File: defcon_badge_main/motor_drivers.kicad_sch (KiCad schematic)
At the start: 14 parts

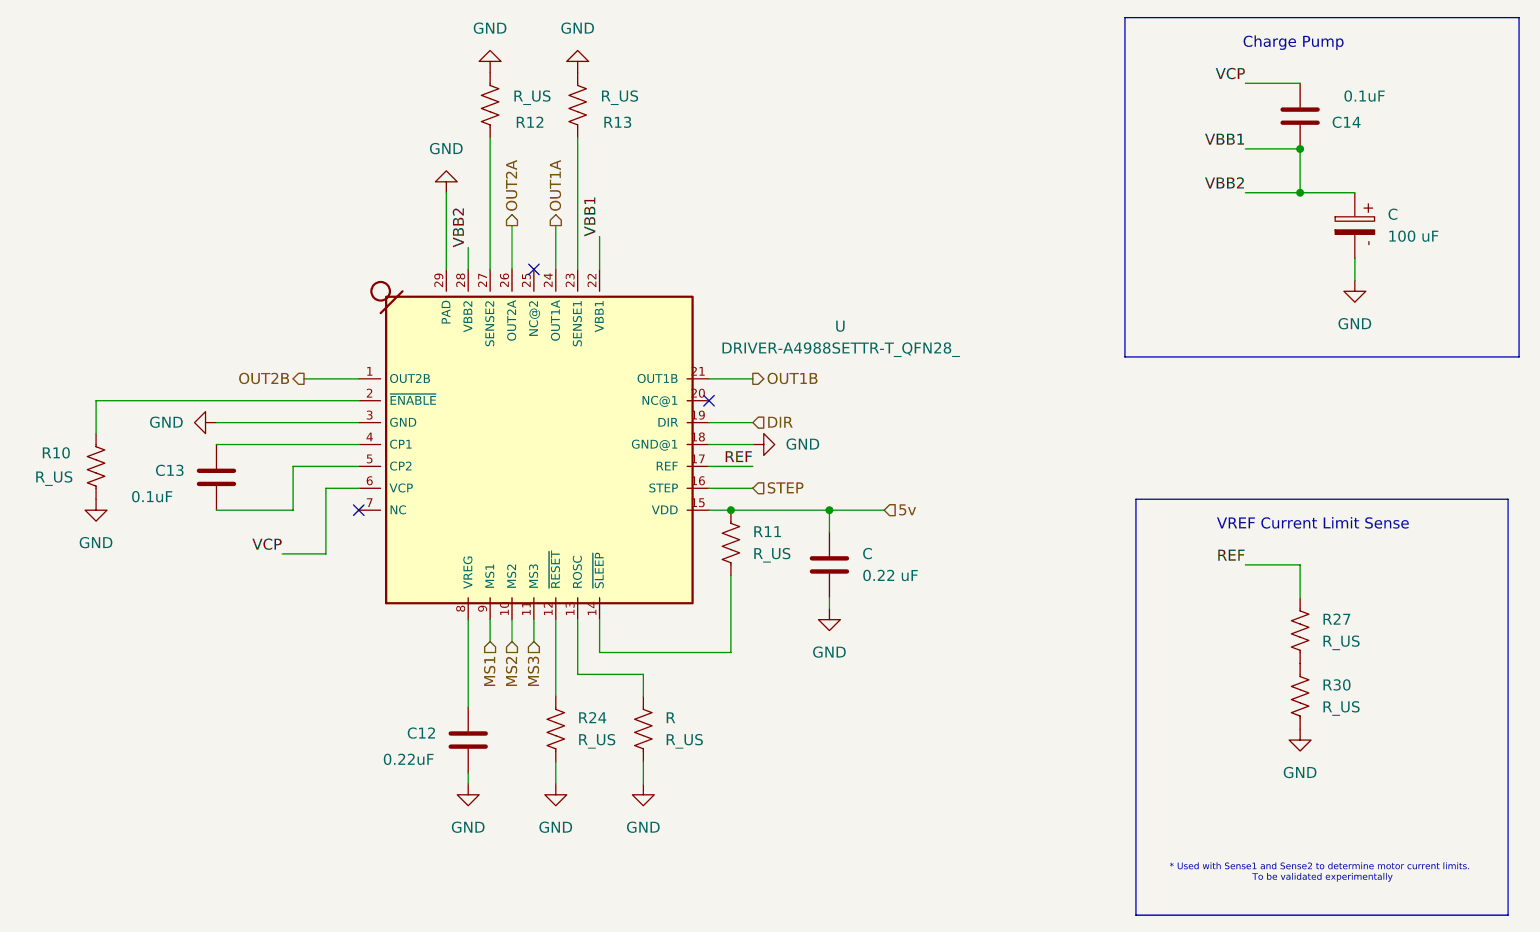
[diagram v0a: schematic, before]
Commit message: ESP32 test board layout
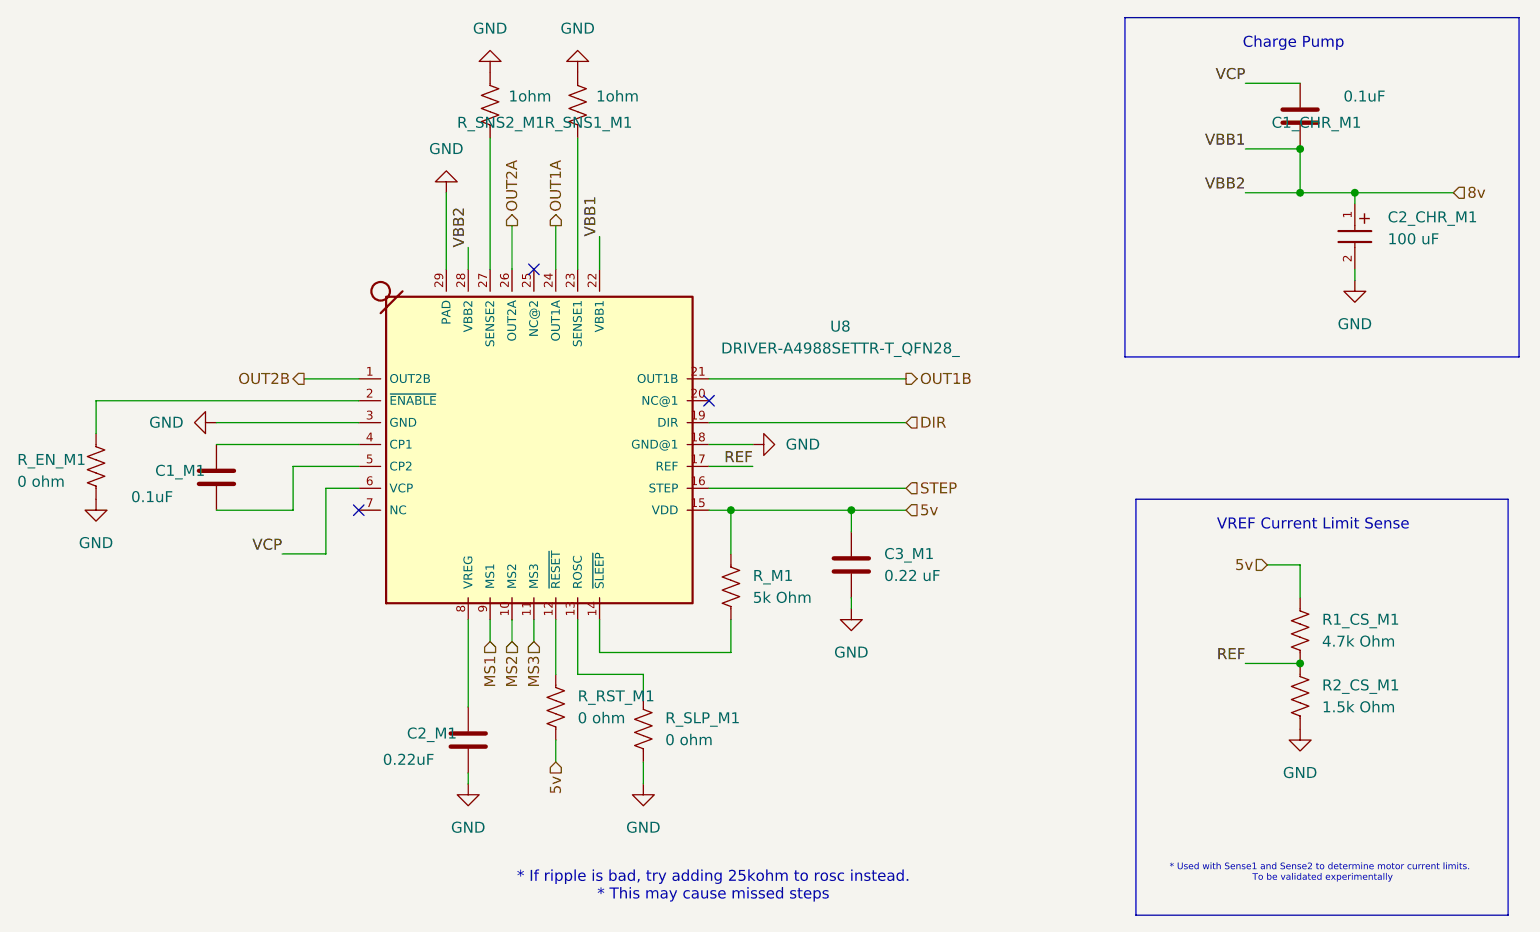
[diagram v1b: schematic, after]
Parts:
- removed C: 100 uF, Capacitor_THT:CP_Radial_D5.0mm_P2.50mm, symbol PCM_SL_Devices:Capacitor_PO
- removed R, R10, R24: R_US, symbol Device:R_US
- added C2_CHR_M1: 100 uF, WCAP-ASLI_6.3X5.5:WCAP-ASLI_6.3X5.5_DXL_, symbol WCAP-ASLI_6.3X5.5:WCAP-ASLI_6.3X5.5
- added R_EN_M1, R_RST_M1, R_SLP_M1: 0 ohm, PCM_SparkFun-Fuse:1206, symbol Device:R_US
- C1_CHR_M1: renamed from C14; footprint (none) -> PCM_SparkFun-Coil:0805
- C1_M1: renamed from C13; footprint (none) -> PCM_SparkFun-Coil:0805
- C2_M1: renamed from C12; footprint (none) -> PCM_SparkFun-Coil:0805
- C3_M1: renamed from C; footprint (none) -> PCM_SparkFun-Coil:0805
- R1_CS_M1: renamed from R27; value R_US -> 4.7k Ohm; footprint (none) -> PCM_SparkFun-Fuse:1206
- R2_CS_M1: renamed from R30; value R_US -> 1.5k Ohm; footprint (none) -> PCM_SparkFun-Fuse:1206
- R_M1: renamed from R11; value R_US -> 5k Ohm; footprint (none) -> PCM_SparkFun-Fuse:1206
- R_SNS1_M1: renamed from R13; value R_US -> 1ohm; footprint (none) -> PCM_SparkFun-Fuse:1206
- R_SNS2_M1: renamed from R12; value R_US -> 1ohm; footprint (none) -> PCM_SparkFun-Fuse:1206
- renumbered U to U8
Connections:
- net 5v: now also R1_CS_M1.1, R_RST_M1.2
- net GND: now also C2_CHR_M1.2, R_EN_M1.2, R_SLP_M1.2
- net REF: now also R1_CS_M1.2, R2_CS_M1.1; no longer R1_CS_M1.1
- net at U8.12 (~{RESET}): now also R_RST_M1.1
- net at U8.2 (~{ENABLE}): now also R_EN_M1.1
- net at U8.13 (ROSC): now also R_SLP_M1.1
- net VBB1 renamed 8v
- net 8v: now also C2_CHR_M1.1
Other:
- note added: "* If ripple is bad, try adding 25kohm to rosc instead. * This may cause missed steps"
- moved on the sheet: C3_M1, R_M1

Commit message: begin full layout
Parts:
- R1_CS_M1, R2_CS_M1, R_EN_M1, R_M1, R_RST_M1, R_SLP_M1, R_SNS1_M1, R_SNS2_M1: footprint PCM_SparkFun-Fuse:1206 -> PCM_SparkFun-Coil:0805
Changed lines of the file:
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@@
 	(wire
 		(pts
-			(xy 74.93 80.01) (xy 81.28 80.01)
+			(xy 73.66 80.01) (xy 81.28 80.01)
 		)
 		(stroke
@@
 	(wire
 		(pts
-			(xy 104.14 62.23) (xy 104.14 67.31)
+			(xy 104.14 59.69) (xy 104.14 67.31)
 		)
 		(stroke
@@
 	(wire
 		(pts
-			(xy 99.06 62.23) (xy 99.06 67.31)
+			(xy 99.06 59.69) (xy 99.06 67.31)
 		)
 		(stroke
@@
 			(width 0)
 			(type default)
+		)
+	)
+	(label "OUT1A"
+		(at 104.14 66.04 90)
+		(effects
+			(font
+				(size 1.27 1.27)
+			)
+			(justify left bottom)
 		)
 	)
@@
 		)
 	)
+	(label "OUT2B"
+		(at 74.93 80.01 0)
+		(effects
+			(font
+				(size 1.27 1.27)
+			)
+			(justify left bottom)
+		)
+	)
+	(label "OUT1B"
+		(at 130.81 80.01 0)
+		(effects
+			(font
+				(size 1.27 1.27)
+			)
+			(justify left bottom)
+		)
+	)
 	(label "VCP"
 		(at 72.39 100.33 180)
@@
 	(label "VBB1"
 		(at 109.22 63.5 90)
+		(effects
+			(font
+				(size 1.27 1.27)
+			)
+			(justify left bottom)
+		)
+	)
+	(label "OUT2A"
+		(at 99.06 66.04 90)
 		(effects
 			(font
@@
 	(hierarchical_label "OUT2B"
 		(shape output)
-		(at 74.93 80.01 180)
+		(at 73.66 80.01 180)
 		(effects
 			(font
@@
 	(hierarchical_label "OUT1A"
 		(shape output)
-		(at 104.14 62.23 90)
+		(at 104.14 59.69 90)
 		(effects
 			(font
@@
 	(hierarchical_label "OUT2A"
 		(shape output)
-		(at 99.06 62.23 90)
+		(at 99.06 59.69 90)
 		(effects
 			(font
@@
 			)
 		)
-		(property "Footprint" "PCM_SparkFun-Fuse:1206"
+		(property "Footprint" "PCM_SparkFun-Coil:0805"
 			(at 191.516 117.094 90)
 			(effects
@@
 			)
 		)
-		(property "Footprint" "PCM_SparkFun-Fuse:1206"
+		(property "Footprint" "PCM_SparkFun-Coil:0805"
 			(at 191.516 109.474 90)
 			(effects
@@
 			)
 		)
-		(property "Footprint" "PCM_SparkFun-Fuse:1206"
+		(property "Footprint" "PCM_SparkFun-Coil:0805"
 			(at 125.476 104.394 90)
 			(effects
@@
 			)
 		)
-		(property "Footprint" "PCM_SparkFun-Fuse:1206"
+		(property "Footprint" "PCM_SparkFun-Coil:0805"
 			(at 95.504 48.006 90)
 			(effects
@@
 			)
 		)
-		(property "Footprint" "PCM_SparkFun-Fuse:1206"
+		(property "Footprint" "PCM_SparkFun-Coil:0805"
 			(at 105.664 48.006 90)
 			(effects
@@
 			)
 		)
-		(property "Footprint" "PCM_SparkFun-Fuse:1206"
+		(property "Footprint" "PCM_SparkFun-Coil:0805"
 			(at 105.156 118.364 90)
 			(effects
@@
 			)
 		)
-		(property "Footprint" "PCM_SparkFun-Fuse:1206"
+		(property "Footprint" "PCM_SparkFun-Coil:0805"
 			(at 51.816 90.424 90)
 			(effects
@@
 			)
 		)
-		(property "Footprint" "PCM_SparkFun-Fuse:1206"
+		(property "Footprint" "PCM_SparkFun-Coil:0805"
 			(at 115.316 120.904 90)
 			(effects

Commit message: more layout
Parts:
- C1_CHR_M1, C1_M1, C2_M1, C3_M1, R1_CS_M1, R2_CS_M1, R_EN_M1, R_M1, R_RST_M1, R_SNS1_M1, R_SNS2_M1: footprint PCM_SparkFun-Coil:0805 -> joystick:R_0603_1608Metric_Pad0.98x0.95mm_HandSolder_MINE
- R_OSC_M1: renamed from R_SLP_M1; footprint PCM_SparkFun-Coil:0805 -> joystick:R_0603_1608Metric_Pad0.98x0.95mm_HandSolder_MINE
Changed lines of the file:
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@@
 			)
 		)
-		(property "Footprint" "PCM_SparkFun-Coil:0805"
+		(property "Footprint" "joystick:R_0603_1608Metric_Pad0.98x0.95mm_HandSolder_MINE"
 			(at 191.516 117.094 90)
 			(effects
@@
 			)
 		)
-		(property "Footprint" "PCM_SparkFun-Coil:0805"
+		(property "Footprint" "joystick:R_0603_1608Metric_Pad0.98x0.95mm_HandSolder_MINE"
 			(at 191.516 109.474 90)
 			(effects
@@
 			)
 		)
-		(property "Footprint" "PCM_SparkFun-Coil:0805"
+		(property "Footprint" "joystick:R_0603_1608Metric_Pad0.98x0.95mm_HandSolder_MINE"
 			(at 139.3952 105.41 0)
 			(effects
@@
 			)
 		)
-		(property "Footprint" "PCM_SparkFun-Coil:0805"
+		(property "Footprint" "joystick:R_0603_1608Metric_Pad0.98x0.95mm_HandSolder_MINE"
 			(at 125.476 104.394 90)
 			(effects
@@
 			)
 		)
-		(property "Footprint" "PCM_SparkFun-Coil:0805"
+		(property "Footprint" "joystick:R_0603_1608Metric_Pad0.98x0.95mm_HandSolder_MINE"
 			(at 95.504 48.006 90)
 			(effects
@@
 			)
 		)
-		(property "Footprint" "PCM_SparkFun-Coil:0805"
+		(property "Footprint" "joystick:R_0603_1608Metric_Pad0.98x0.95mm_HandSolder_MINE"
 			(at 105.664 48.006 90)
 			(effects
@@
 			)
 		)
-		(property "Footprint" "PCM_SparkFun-Coil:0805"
+		(property "Footprint" "joystick:R_0603_1608Metric_Pad0.98x0.95mm_HandSolder_MINE"
 			(at 93.0148 118.11 0)
 			(effects
@@
 			)
 		)
-		(property "Footprint" "PCM_SparkFun-Coil:0805"
+		(property "Footprint" "joystick:R_0603_1608Metric_Pad0.98x0.95mm_HandSolder_MINE"
 			(at 63.8048 87.63 0)
 			(effects
@@
 			)
 		)
-		(property "Footprint" "PCM_SparkFun-Coil:0805"
+		(property "Footprint" "joystick:R_0603_1608Metric_Pad0.98x0.95mm_HandSolder_MINE"
 			(at 105.156 118.364 90)
 			(effects
@@
 			)
 		)
-		(property "Footprint" "PCM_SparkFun-Coil:0805"
+		(property "Footprint" "joystick:R_0603_1608Metric_Pad0.98x0.95mm_HandSolder_MINE"
 			(at 51.816 90.424 90)
 			(effects
@@
 		(dnp no)
 		(fields_autoplaced yes)
-		(property "Reference" "R_SLP_M1"
+		(property "Reference" "R_OSC_M1"
 			(at 116.84 119.3799 0)
 			(effects
@@
 			)
 		)
-		(property "Footprint" "PCM_SparkFun-Coil:0805"
+		(property "Footprint" "joystick:R_0603_1608Metric_Pad0.98x0.95mm_HandSolder_MINE"
 			(at 115.316 120.904 90)
 			(effects
@@
 			(project "defcon_badge_main"
 				(path "/b497f1e3-23b9-4176-bc4d-bc3995ba532c/80ac077f-60b7-46ed-9cae-89df459cc96b"
-					(reference "R_SLP_M3")
-					(unit 1)
-				)
-				(path "/b497f1e3-23b9-4176-bc4d-bc3995ba532c/c0b9f135-7457-46a3-ba59-e1dcc8eab596"
-					(reference "R_SLP_M2")
-					(unit 1)
-				)
-				(path "/b497f1e3-23b9-4176-bc4d-bc3995ba532c/fa42b96d-02fc-4c50-9821-483af63ffede"
-					(reference "R_SLP_M1")
+					(reference "R_OSC_M3")
+					(unit 1)
+				)
+				(path "/b497f1e3-23b9-4176-bc4d-bc3995ba532c/c0b9f135-7457-46a3-ba59-e1dcc8eab596"
+					(reference "R_OSC_M2")
+					(unit 1)
+				)
+				(path "/b497f1e3-23b9-4176-bc4d-bc3995ba532c/fa42b96d-02fc-4c50-9821-483af63ffede"
+					(reference "R_OSC_M1")
 					(unit 1)
 				)
@@
 			)
 		)
-		(property "Footprint" "PCM_SparkFun-Coil:0805"
+		(property "Footprint" "joystick:R_0603_1608Metric_Pad0.98x0.95mm_HandSolder_MINE"
 			(at 191.4652 53.34 0)
 			(effects

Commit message: added component parts and modifications
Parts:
- C1_CHR_M1, C1_M1: MPN (none) -> GMC10X7R104M16NTD; Rating (none) -> 16V
- C2_CHR_M1: MPN (none) -> 865080343009
- C2_M1, C3_M1: MPN (none) -> GMC10X5R224K25NT; Rating (none) -> 16V
- R1_CS_M1: MPN (none) -> RM06J472CT; TOL (none) -> 5%
- R2_CS_M1: MPN (none) -> RM06F1501CT
- R_EN_M1, R_OSC_M1, R_RST_M1: MPN (none) -> RM06J000CT
- R_M1: MPN (none) -> MCT06030D5001BP500; TOL (none) -> 0.1%
- R_SNS1_M1, R_SNS2_M1: value 1ohm -> 1 Ohm; MPN (none) -> RM06J1R0CT
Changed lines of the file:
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@@
 			)
 		)
-		(property "Datasheet" "~"
+		(property "Datasheet" "https://calchip.com/wp-content/uploads/2025/05/RMSERIES-052225.pdf"
 			(at 190.5 116.84 0)
 			(effects
@@
 		)
 		(property "Description" "Resistor, US symbol"
+			(at 190.5 116.84 0)
+			(effects
+				(font
+					(size 1.27 1.27)
+				)
+				(hide yes)
+			)
+		)
+		(property "MPN" "RM06F1501CT"
 			(at 190.5 116.84 0)
 			(effects
@@
 			)
 		)
-		(property "Datasheet" "~"
+		(property "Datasheet" "https://calchip.com/wp-content/uploads/2025/05/RMSERIES-052225.pdf"
 			(at 190.5 109.22 0)
 			(effects
@@
 		)
 		(property "Description" "Resistor, US symbol"
+			(at 190.5 109.22 0)
+			(effects
+				(font
+					(size 1.27 1.27)
+				)
+				(hide yes)
+			)
+		)
+		(property "MPN" "RM06J472CT"
+			(at 190.5 109.22 0)
+			(effects
+				(font
+					(size 1.27 1.27)
+				)
+				(hide yes)
+			)
+		)
+		(property "TOL" "5%"
 			(at 190.5 109.22 0)
 			(effects
@@
 			)
 		)
-		(property "Datasheet" "~"
+		(property "Datasheet" "https://calchip.com/wp-content/uploads/2025/05/GMC-Series-3.pdf"
 			(at 138.43 101.6 0)
 			(effects
@@
 		)
 		(property "Description" "Unpolarized capacitor"
+			(at 138.43 101.6 0)
+			(effects
+				(font
+					(size 1.27 1.27)
+				)
+				(hide yes)
+			)
+		)
+		(property "MPN" "GMC10X5R224K25NT"
+			(at 138.43 101.6 0)
+			(effects
+				(font
+					(size 1.27 1.27)
+				)
+				(hide yes)
+			)
+		)
+		(property "Rating" "16V"
 			(at 138.43 101.6 0)
 			(effects
@@
 			)
 		)
-		(property "Datasheet" "~"
+		(property "Datasheet" "https://www.vishay.com/docs/28700/mcx0x0xpre.pdf"
 			(at 124.46 104.14 0)
 			(effects
@@
 			)
 		)
+		(property "MPN" "MCT06030D5001BP500"
+			(at 124.46 104.14 0)
+			(effects
+				(font
+					(size 1.27 1.27)
+				)
+				(hide yes)
+			)
+		)
+		(property "TOL" "0.1%"
+			(at 124.46 104.14 0)
+			(effects
+				(font
+					(size 1.27 1.27)
+				)
+				(hide yes)
+			)
+		)
 		(pin "2"
 		)
@@
 			)
 		)
-		(property "Value" "1ohm"
+		(property "Value" "1 Ohm"
 			(at 103.632 47.244 0)
 			(effects
@@
 			)
 		)
-		(property "Datasheet" "~"
+		(property "Datasheet" "https://calchip.com/wp-content/uploads/2025/05/RMSERIES-052225.pdf"
 			(at 96.52 48.26 0)
 			(effects
@@
 		)
 		(property "Description" "Resistor, US symbol"
+			(at 96.52 48.26 0)
+			(effects
+				(font
+					(size 1.27 1.27)
+				)
+				(hide yes)
+			)
+		)
+		(property "MPN" "RM06J1R0CT"
 			(at 96.52 48.26 0)
 			(effects
@@
 			)
 		)
-		(property "Datasheet" ""
+		(property "Datasheet" "https://www.allegromicro.com/-/media/files/datasheets/a4988-datasheet.pdf"
 			(at 101.6 87.63 0)
 			(effects
@@
 			)
 		)
-		(property "Value" "1ohm"
+		(property "Value" "1 Ohm"
 			(at 113.792 47.244 0)
 			(effects
@@
 			)
 		)
-		(property "Datasheet" "~"
+		(property "Datasheet" "https://calchip.com/wp-content/uploads/2025/05/RMSERIES-052225.pdf"
 			(at 106.68 48.26 0)
 			(effects
@@
 		)
 		(property "Description" "Resistor, US symbol"
+			(at 106.68 48.26 0)
+			(effects
+				(font
+					(size 1.27 1.27)
+				)
+				(hide yes)
+			)
+		)
+		(property "MPN" "RM06J1R0CT"
 			(at 106.68 48.26 0)
 			(effects
@@
 			)
 		)
-		(property "Datasheet" ""
+		(property "Datasheet" "https://www.we-online.com/components/products/datasheet/865080343009.pdf"
 			(at 196.85 64.77 0)
 			(effects
@@
 				)
 				(justify bottom)
+				(hide yes)
+			)
+		)
+		(property "MPN" "865080343009"
+			(at 196.85 64.77 90)
+			(effects
+				(font
+					(size 1.27 1.27)
+				)
 				(hide yes)
 			)
@@
 			)
 		)
-		(property "Datasheet" "~"
+		(property "Datasheet" "https://calchip.com/wp-content/uploads/2025/05/GMC-Series-3.pdf"
 			(at 93.98 121.92 0)
 			(effects
@@
 		)
 		(property "Description" "Unpolarized capacitor"
+			(at 93.98 121.92 0)
+			(effects
+				(font
+					(size 1.27 1.27)
+				)
+				(hide yes)
+			)
+		)
+		(property "MPN" "GMC10X5R224K25NT"
+			(at 93.98 121.92 0)
+			(effects
+				(font
+					(size 1.27 1.27)
+				)
+				(hide yes)
+			)
+		)
+		(property "Rating" "16V"
 			(at 93.98 121.92 0)
 			(effects
@@
 			)
 		)
-		(property "Datasheet" "~"
+		(property "Datasheet" "https://calchip.com/wp-content/uploads/2025/05/GMC-Series-3.pdf"
 			(at 64.77 91.44 0)
 			(effects
@@
 		)
 		(property "Description" "Unpolarized capacitor"
+			(at 64.77 91.44 0)
+			(effects
+				(font
+					(size 1.27 1.27)
+				)
+				(hide yes)
+			)
+		)
+		(property "MPN" "GMC10X7R104M16NTD"
+			(at 64.77 91.44 0)
+			(effects
+				(font
+					(size 1.27 1.27)
+				)
+				(hide yes)
+			)
+		)
+		(property "Rating" "16V"
 			(at 64.77 91.44 0)
 			(effects
@@
 			)
 		)
-		(property "Datasheet" "~"
+		(property "Datasheet" "https://calchip.com/wp-content/uploads/2025/05/RMSERIES-052225.pdf"
 			(at 104.14 118.11 0)
 			(effects
@@
 			)
 		)
+		(property "MPN" "RM06J000CT"
+			(at 104.14 118.11 0)
+			(effects
+				(font
+					(size 1.27 1.27)
+				)
+				(hide yes)
+			)
+		)
 		(pin "2"
 		)
@@
 			)
 		)
-		(property "Datasheet" "~"
+		(property "Datasheet" "https://calchip.com/wp-content/uploads/2025/05/RMSERIES-052225.pdf"
 			(at 50.8 90.17 0)
 			(effects
@@
 		)
 		(property "Description" "Resistor, US symbol"
+			(at 50.8 90.17 0)
+			(effects
+				(font
+					(size 1.27 1.27)
+				)
+				(hide yes)
+			)
+		)
+		(property "MPN" "RM06J000CT"
 			(at 50.8 90.17 0)
 			(effects
@@
 			)
 		)
-		(property "Datasheet" "~"
+		(property "Datasheet" "https://calchip.com/wp-content/uploads/2025/05/RMSERIES-052225.pdf"
 			(at 114.3 120.65 0)
 			(effects
@@
 		)
 		(property "Description" "Resistor, US symbol"
+			(at 114.3 120.65 0)
+			(effects
+				(font
+					(size 1.27 1.27)
+				)
+				(hide yes)
+			)
+		)
+		(property "MPN" "RM06J000CT"
 			(at 114.3 120.65 0)
 			(effects
@@
 			)
 		)
-		(property "Datasheet" "~"
+		(property "Datasheet" "https://calchip.com/wp-content/uploads/2025/05/GMC-Series-3.pdf"
 			(at 190.5 49.53 0)
 			(effects
@@
 			(at 190.5 49.53 0)
 			(effects
+				(font
+					(size 1.27 1.27)
+				)
+				(hide yes)
+			)
+		)
+		(property "MPN" "GMC10X7R104M16NTD"
+			(at 190.5 49.53 0)
+			(effects
+				(font
+					(size 1.27 1.27)
+				)
+				(hide yes)
+			)
+		)
+		(property "Rating" "16V"
+			(at 190.5 49.53 0)
+			(effects
